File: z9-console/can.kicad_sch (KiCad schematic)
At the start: 8 parts, among them J3 JST GH, J6 Screw_Terminal_01x06, U2 ISO1042-Q1

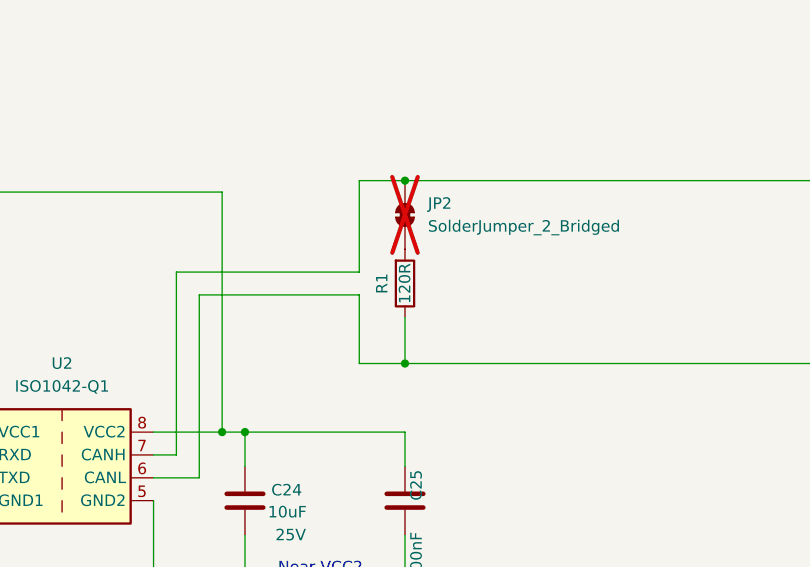
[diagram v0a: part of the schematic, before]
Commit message: lcd power switch-- add new accelerometer
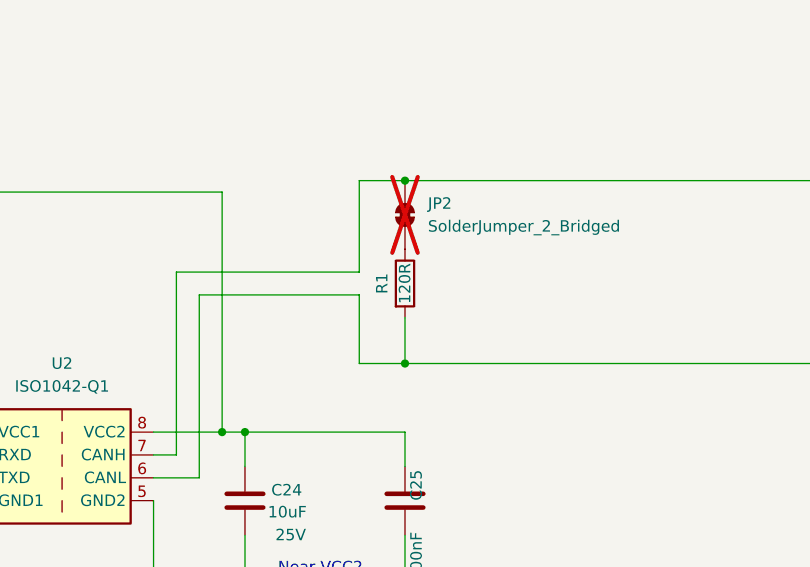
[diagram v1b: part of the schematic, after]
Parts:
- R1: footprint Resistor_SMD:R_0805_2012Metric -> PCM_JLCPCB:R_0402; symbol Device:R -> dnt_global:Resistor_0402,10kΩ; Attrition Qty (none) -> 10; Category (none) -> Resistors,Chip Resistor - Surface Mount; Class (none) -> Basic Component; LCSC C17437 -> C25744; Manufacturer (none) -> UNI-ROYAL(Uniroyal Elec); Minimum Qty (none) -> 20; Operating Temperature Range (none) -> -55°C~+155°C; Overload Voltage (Max) (none) -> 50V; Part (none) -> 0402WGF1002TCE; Power(Watts) (none) -> 62.5mW; Price (none) -> 0.004USD; Process (none) -> SMT; Resistance (none) -> 10kΩ; Stock (none) -> 24372091; Temperature Coefficient (none) -> ±100ppm/°C; Tolerance (none) -> ±1%; Type (none) -> Thick Film Resistors
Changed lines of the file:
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@@
 	)
 	(symbol
-		(lib_id "Device:R")
+		(lib_id "dnt_global:Resistor_0402,10kΩ")
 		(at 135.89 90.17 0)
 		(mirror x)
@@
 			)
 		)
-		(property "Footprint" "Resistor_SMD:R_0805_2012Metric"
+		(property "Footprint" "PCM_JLCPCB:R_0402"
 			(at 134.112 90.17 90)
 			(effects
@@
 			)
 		)
-		(property "Datasheet" "https://wmsc.lcsc.com/wmsc/upload/file/pdf/v2/lcsc/2206010216_UNI-ROYAL-Uniroyal-Elec-0805W8F1200T5E_C17437.pdf"
-			(at 135.89 90.17 0)
-			(effects
-				(font
-					(size 1.27 1.27)
-				)
-				(hide yes)
-			)
-		)
-		(property "Description" "Resistor"
-			(at 135.89 90.17 0)
-			(effects
-				(font
-					(size 1.27 1.27)
-				)
-				(hide yes)
-			)
-		)
-		(property "LCSC" "C17437"
-			(at 135.89 90.17 90)
-			(effects
-				(font
-					(size 1.27 1.27)
-				)
-				(hide yes)
-			)
-		)
-		(property "Sim.Device" ""
-			(at 135.89 90.17 0)
-			(effects
-				(font
-					(size 1.27 1.27)
-				)
-				(hide yes)
-			)
-		)
-		(property "Sim.Pins" ""
-			(at 135.89 90.17 0)
-			(effects
-				(font
-					(size 1.27 1.27)
-				)
-				(hide yes)
-			)
-		)
-		(property "Silkscreen" ""
-			(at 135.89 90.17 0)
-			(effects
+		(property "Datasheet" "https://www.lcsc.com/datasheet/lcsc_datasheet_2411221126_UNI-ROYAL-Uniroyal-Elec-0402WGF1002TCE_C25744.pdf"
+			(at 135.89 90.17 0)
+			(effects
+				(font
+					(size 1.27 1.27)
+				)
+				(hide yes)
+			)
+		)
+		(property "Description" "62.5mW Thick Film Resistors 50V ±100ppm/°C ±1% 10kΩ 0402 Chip Resistor - Surface Mount ROHS"
+			(at 135.89 90.17 0)
+			(effects
+				(font
+					(size 1.27 1.27)
+				)
+				(hide yes)
+			)
+		)
+		(property "LCSC" "C25744"
+			(at 135.89 90.17 0)
+			(effects
+				(font
+					(size 1.27 1.27)
+				)
+				(hide yes)
+			)
+		)
+		(property "Stock" "24372091"
+			(at 135.89 90.17 0)
+			(effects
+				(font
+					(size 1.27 1.27)
+				)
+				(hide yes)
+			)
+		)
+		(property "Price" "0.004USD"
+			(at 135.89 90.17 0)
+			(effects
+				(font
+					(size 1.27 1.27)
+				)
+				(hide yes)
+			)
+		)
+		(property "Process" "SMT"
+			(at 135.89 90.17 0)
+			(effects
+				(font
+					(size 1.27 1.27)
+				)
+				(hide yes)
+			)
+		)
+		(property "Minimum Qty" "20"
+			(at 135.89 90.17 0)
+			(effects
+				(font
+					(size 1.27 1.27)
+				)
+				(hide yes)
+			)
+		)
+		(property "Attrition Qty" "10"
+			(at 135.89 90.17 0)
+			(effects
+				(font
+					(size 1.27 1.27)
+				)
+				(hide yes)
+			)
+		)
+		(property "Class" "Basic Component"
+			(at 135.89 90.17 0)
+			(effects
+				(font
+					(size 1.27 1.27)
+				)
+				(hide yes)
+			)
+		)
+		(property "Category" "Resistors,Chip Resistor - Surface Mount"
+			(at 135.89 90.17 0)
+			(effects
+				(font
+					(size 1.27 1.27)
+				)
+				(hide yes)
+			)
+		)
+		(property "Manufacturer" "UNI-ROYAL(Uniroyal Elec)"
+			(at 135.89 90.17 0)
+			(effects
+				(font
+					(size 1.27 1.27)
+				)
+				(hide yes)
+			)
+		)
+		(property "Part" "0402WGF1002TCE"
+			(at 135.89 90.17 0)
+			(effects
+				(font
+					(size 1.27 1.27)
+				)
+				(hide yes)
+			)
+		)
+		(property "Resistance" "10kΩ"
+			(at 135.89 90.17 0)
+			(effects
+				(font
+					(size 1.27 1.27)
+				)
+				(hide yes)
+			)
+		)
+		(property "Power(Watts)" "62.5mW"
+			(at 135.89 90.17 0)
+			(effects
+				(font
+					(size 1.27 1.27)
+				)
+				(hide yes)
+			)
+		)
+		(property "Type" "Thick Film Resistors"
+			(at 135.89 90.17 0)
+			(effects
+				(font
+					(size 1.27 1.27)
+				)
+				(hide yes)
+			)
+		)
+		(property "Overload Voltage (Max)" "50V"
+			(at 135.89 90.17 0)
+			(effects
+				(font
+					(size 1.27 1.27)
+				)
+				(hide yes)
+			)
+		)
+		(property "Operating Temperature Range" "-55°C~+155°C"
+			(at 135.89 90.17 0)
+			(effects
+				(font
+					(size 1.27 1.27)
+				)
+				(hide yes)
+			)
+		)
+		(property "Tolerance" "±1%"
+			(at 135.89 90.17 0)
+			(effects
+				(font
+					(size 1.27 1.27)
+				)
+				(hide yes)
+			)
+		)
+		(property "Temperature Coefficient" "±100ppm/°C"
+			(at 135.89 90.17 0)
+			(effects

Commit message: change MEMS device
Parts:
- R20: renamed from R1; footprint PCM_JLCPCB:R_0402 -> dnt:R_1206_3216Metric; symbol dnt_global:Resistor_0402,10kΩ -> dnt_global:Resistor_-_1206,120Ω; LCSC C25744 -> C17909; Minimum Qty 20 -> 15; Overload Voltage (Max) 50V -> 200V; Part 0402WGF1002TCE -> 1206W4F1200T5E; Power(Watts) 62.5mW -> 250mW; Price 0.004USD -> 0.007USD; Resistance 10kΩ -> 120Ω; Stock 24372091 -> 622568
- renumbered C22 to C25, C24 to C26, C25 to C27, J6 to J10, J3 to J9, JP2 to JP3, U2 to U9
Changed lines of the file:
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@@
 		(dnp no)
 		(fields_autoplaced yes)
-		(property "Reference" "#PWR05"
+		(property "Reference" "#PWR043"
 			(at 44.45 124.46 0)
 			(effects
@@
 			(project "l8-kicad"
 				(path "/8d063f79-9282-4820-bcf4-1ff3c006cf08/73909d3a-f2e9-43a1-adfe-e0aaff309cf7"
-					(reference "#PWR05")
+					(reference "#PWR043")
 					(unit 1)
 				)
@@
 		(on_board yes)
 		(dnp no)
-		(property "Reference" "C25"
+		(property "Reference" "C27"
 			(at 137.16 114.3 90)
 			(effects
@@
 			)
 		)
-		(property "Datasheet" "https://wmsc.lcsc.com/wmsc/upload/file/pdf/v2/lcsc/2211101700_YAGEO-CC0603KRX7R9BB104_C14663.pdf"
+		(property "Datasheet" "~"
 			(at 135.89 114.3 0)
 			(effects
@@
 			)
 		)
-		(property "Description" "50V 100nF X7R ±10% 0603 Multilayer Ceramic Capacitors MLCC - SMD/SMT ROHS"
+		(property "Description" "Unpolarized capacitor"
 			(at 135.89 114.3 0)
 			(effects
@@
 			(project "l8-kicad"
 				(path "/8d063f79-9282-4820-bcf4-1ff3c006cf08/73909d3a-f2e9-43a1-adfe-e0aaff309cf7"
-					(reference "C25")
+					(reference "C27")
 					(unit 1)
 				)
@@
 	)
 	(symbol
-		(lib_id "dnt_global:Resistor_0402,10kΩ")
+		(lib_id "dnt_global:Resistor_-_1206,120Ω")
 		(at 135.89 90.17 0)
 		(mirror x)
@@
 		(on_board yes)
 		(dnp no)
-		(property "Reference" "R1"
+		(property "Reference" "R20"
 			(at 133.35 90.17 90)
 			(effects
@@
 			)
 		)
-		(property "Footprint" "PCM_JLCPCB:R_0402"
+		(property "Footprint" "dnt:R_1206_3216Metric"
 			(at 134.112 90.17 90)
 			(effects
@@
 			)
 		)
-		(property "Datasheet" "https://www.lcsc.com/datasheet/lcsc_datasheet_2411221126_UNI-ROYAL-Uniroyal-Elec-0402WGF1002TCE_C25744.pdf"
-			(at 135.89 90.17 0)
-			(effects
-				(font
-					(size 1.27 1.27)
-				)
-				(hide yes)
-			)
-		)
-		(property "Description" "62.5mW Thick Film Resistors 50V ±100ppm/°C ±1% 10kΩ 0402 Chip Resistor - Surface Mount ROHS"
-			(at 135.89 90.17 0)
-			(effects
-				(font
-					(size 1.27 1.27)
-				)
-				(hide yes)
-			)
-		)
-		(property "LCSC" "C25744"
-			(at 135.89 90.17 0)
-			(effects
-				(font
-					(size 1.27 1.27)
-				)
-				(hide yes)
-			)
-		)
-		(property "Stock" "24372091"
-			(at 135.89 90.17 0)
-			(effects
-				(font
-					(size 1.27 1.27)
-				)
-				(hide yes)
-			)
-		)
-		(property "Price" "0.004USD"
+		(property "Datasheet" "https://www.lcsc.com/datasheet/lcsc_datasheet_2206010145_UNI-ROYAL-Uniroyal-Elec-1206W4F1200T5E_C17909.pdf"
+			(at 135.89 90.17 0)
+			(effects
+				(font
+					(size 1.27 1.27)
+				)
+				(hide yes)
+			)
+		)
+		(property "Description" "250mW Thick Film Resistors 200V ±100ppm/°C ±1% 120Ω 1206 Chip Resistor - Surface Mount ROHS"
+			(at 135.89 90.17 0)
+			(effects
+				(font
+					(size 1.27 1.27)
+				)
+				(hide yes)
+			)
+		)
+		(property "LCSC" "C17909"
+			(at 135.89 90.17 0)
+			(effects
+				(font
+					(size 1.27 1.27)
+				)
+				(hide yes)
+			)
+		)
+		(property "Stock" "622568"
+			(at 135.89 90.17 0)
+			(effects
+				(font
+					(size 1.27 1.27)
+				)
+				(hide yes)
+			)
+		)
+		(property "Price" "0.007USD"
 			(at 135.89 90.17 0)
 			(effects
@@
 			)
 		)
-		(property "Minimum Qty" "20"
+		(property "Minimum Qty" "15"
 			(at 135.89 90.17 0)
 			(effects
@@
 			)
 		)
-		(property "Part" "0402WGF1002TCE"
-			(at 135.89 90.17 0)
-			(effects
-				(font
-					(size 1.27 1.27)
-				)
-				(hide yes)
-			)
-		)
-		(property "Resistance" "10kΩ"
-			(at 135.89 90.17 0)
-			(effects
-				(font
-					(size 1.27 1.27)
-				)
-				(hide yes)
-			)
-		)
-		(property "Power(Watts)" "62.5mW"
+		(property "Part" "1206W4F1200T5E"
+			(at 135.89 90.17 0)
+			(effects
+				(font
+					(size 1.27 1.27)
+				)
+				(hide yes)
+			)
+		)
+		(property "Resistance" "120Ω"
+			(at 135.89 90.17 0)
+			(effects
+				(font
+					(size 1.27 1.27)
+				)
+				(hide yes)
+			)
+		)
+		(property "Power(Watts)" "250mW"
 			(at 135.89 90.17 0)
 			(effects
@@
 			)
 		)
-		(property "Overload Voltage (Max)" "50V"
+		(property "Overload Voltage (Max)" "200V"
 			(at 135.89 90.17 0)
 			(effects
@@
 			(project "l8-kicad"
 				(path "/8d063f79-9282-4820-bcf4-1ff3c006cf08/73909d3a-f2e9-43a1-adfe-e0aaff309cf7"
-					(reference "R1")
+					(reference "R20")
 					(unit 1)
 				)
@@
 		(on_board yes)
 		(dnp no)
-		(property "Reference" "C22"
+		(property "Reference" "C25"
 			(at 81.28 96.52 90)
 			(effects
@@
 			)
 		)
-		(property "Datasheet" "https://wmsc.lcsc.com/wmsc/upload/file/pdf/v2/lcsc/2211101700_YAGEO-CC0603KRX7R9BB104_C14663.pdf"
+		(property "Datasheet" "~"
 			(at 80.01 97.79 0)
 			(effects
@@
 			)
 		)
-		(property "Description" "50V 100nF X7R ±10% 0603 Multilayer Ceramic Capacitors MLCC - SMD/SMT ROHS"
+		(property "Description" "Unpolarized capacitor"
 			(at 80.01 97.79 0)
 			(effects
@@
 			(project "l8-kicad"
 				(path "/8d063f79-9282-4820-bcf4-1ff3c006cf08/73909d3a-f2e9-43a1-adfe-e0aaff309cf7"
-					(reference "C22")
+					(reference "C25")
 					(unit 1)
 				)
@@
 		(on_board yes)
 		(dnp no)
-		(property "Reference" "C24"
+		(property "Reference" "C26"
 			(at 121.031 113.1316 0)
 			(effects
@@
 			)
 		)
-		(property "Datasheet" ""
+		(property "Datasheet" "~"
 			(at 118.11 114.3 0)
 			(effects
@@
 			)
 		)
-		(property "Description" "X5R"
+		(property "Description" "Unpolarized capacitor"
 			(at 118.11 114.3 0)
 			(effects
@@
 			(project "l8-kicad"
 				(path "/8d063f79-9282-4820-bcf4-1ff3c006cf08/73909d3a-f2e9-43a1-adfe-e0aaff309cf7"
-					(reference "C24")
+					(reference "C26")
 					(unit 1)
 				)
@@
 		(dnp no)
 		(fields_autoplaced yes)
-		(property "Reference" "#PWR026"
+		(property "Reference" "#PWR042"
 			(at 46.99 91.44 0)
 			(effects
@@
 			(project ""
 				(path "/8d063f79-9282-4820-bcf4-1ff3c006cf08/73909d3a-f2e9-43a1-adfe-e0aaff309cf7"
-					(reference "#PWR026")
+					(reference "#PWR042")
 					(unit 1)
 				)
@@
 		(dnp no)
 		(fields_autoplaced yes)
-		(property "Reference" "#PWR014"
+		(property "Reference" "#PWR044"
 			(at 219.71 154.94 0)
 			(effects
@@
 			(project "l8-kicad"
 				(path "/8d063f79-9282-4820-bcf4-1ff3c006cf08/73909d3a-f2e9-43a1-adfe-e0aaff309cf7"
-					(reference "#PWR014")
+					(reference "#PWR044")
 					(unit 1)
 				)
@@
 		(dnp no)
 		(fields_autoplaced yes)
-		(property "Reference" "J3"
+		(property "Reference" "J9"
 			(at 251.46 73.66 0)
 			(effects
@@
 			(project "l8-kicad"
 				(path "/8d063f79-9282-4820-bcf4-1ff3c006cf08/73909d3a-f2e9-43a1-adfe-e0aaff309cf7"
-					(reference "J3")
+					(reference "J9")
 					(unit 1)
 				)
@@
 		(dnp no)
 		(fields_autoplaced yes)
-		(property "Reference" "J6"
+		(property "Reference" "J10"
 			(at 251.46 97.79 0)
 			(effects
@@
 			(project "l8-kicad"
 				(path "/8d063f79-9282-4820-bcf4-1ff3c006cf08/73909d3a-f2e9-43a1-adfe-e0aaff309cf7"
-					(reference "J6")
+					(reference "J10")
 					(unit 1)
 				)
@@
 		(dnp yes)
 		(fields_autoplaced yes)
-		(property "Reference" "JP2"
+		(property "Reference" "JP3"
 			(at 138.43 81.2799 90)
 			(effects
@@
 			(project "l8-kicad"
 				(path "/8d063f79-9282-4820-bcf4-1ff3c006cf08/73909d3a-f2e9-43a1-adfe-e0aaff309cf7"
-					(reference "JP2")
+					(reference "JP3")
 					(unit 1)
 				)
@@
 		(dnp no)
 		(fields_autoplaced yes)
-		(property "Reference" "U2"
+		(property "Reference" "U9"
 			(at 97.79 99.06 0)
 			(effects
@@
 			(project "l8-kicad"
 				(path "/8d063f79-9282-4820-bcf4-1ff3c006cf08/73909d3a-f2e9-43a1-adfe-e0aaff309cf7"
-					(reference "U2")
+					(reference "U9")
 					(unit 1)
 				)
